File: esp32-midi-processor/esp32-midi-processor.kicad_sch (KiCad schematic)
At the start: 50 parts, among them J1 Midi IN 1, J10 USB Shield right, J11 Spare, J12 Display, J2 Midi IN 2, J3 Midi OUT 1, J4 Midi OUT 2, J5 ESP32 right, J6 ESP32 left, J7 Input Voltage, J8 USB Shield outer left, J9 USB Shield inner left, SW1 SW_Push, SW2 SW_Push, SW3 SW_Push, SW4 SW_Push, SW5 RotaryEncoder_Switch, U1 6N138, U2 6N138

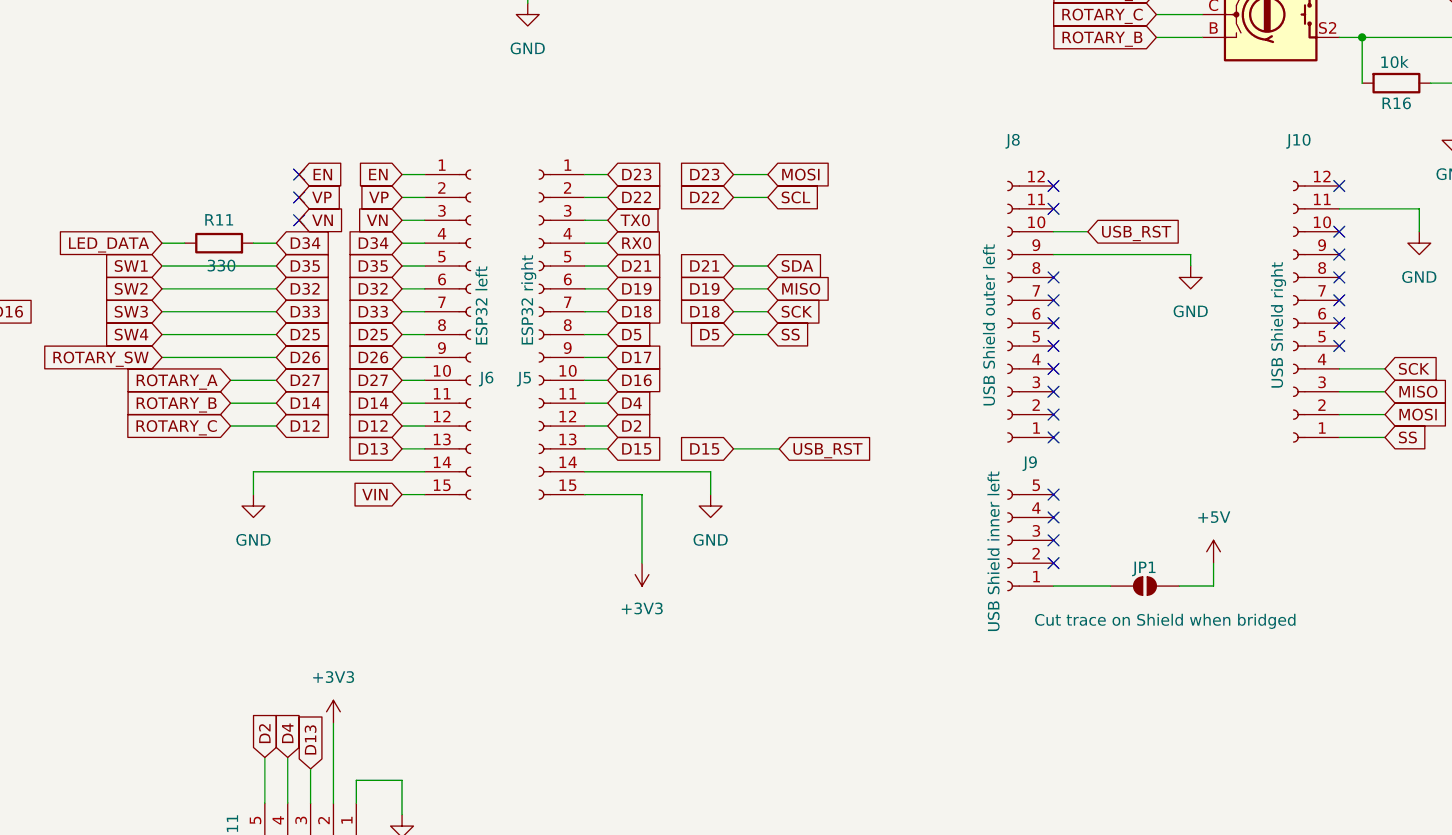
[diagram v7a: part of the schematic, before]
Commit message: fix orientation of pinheaders
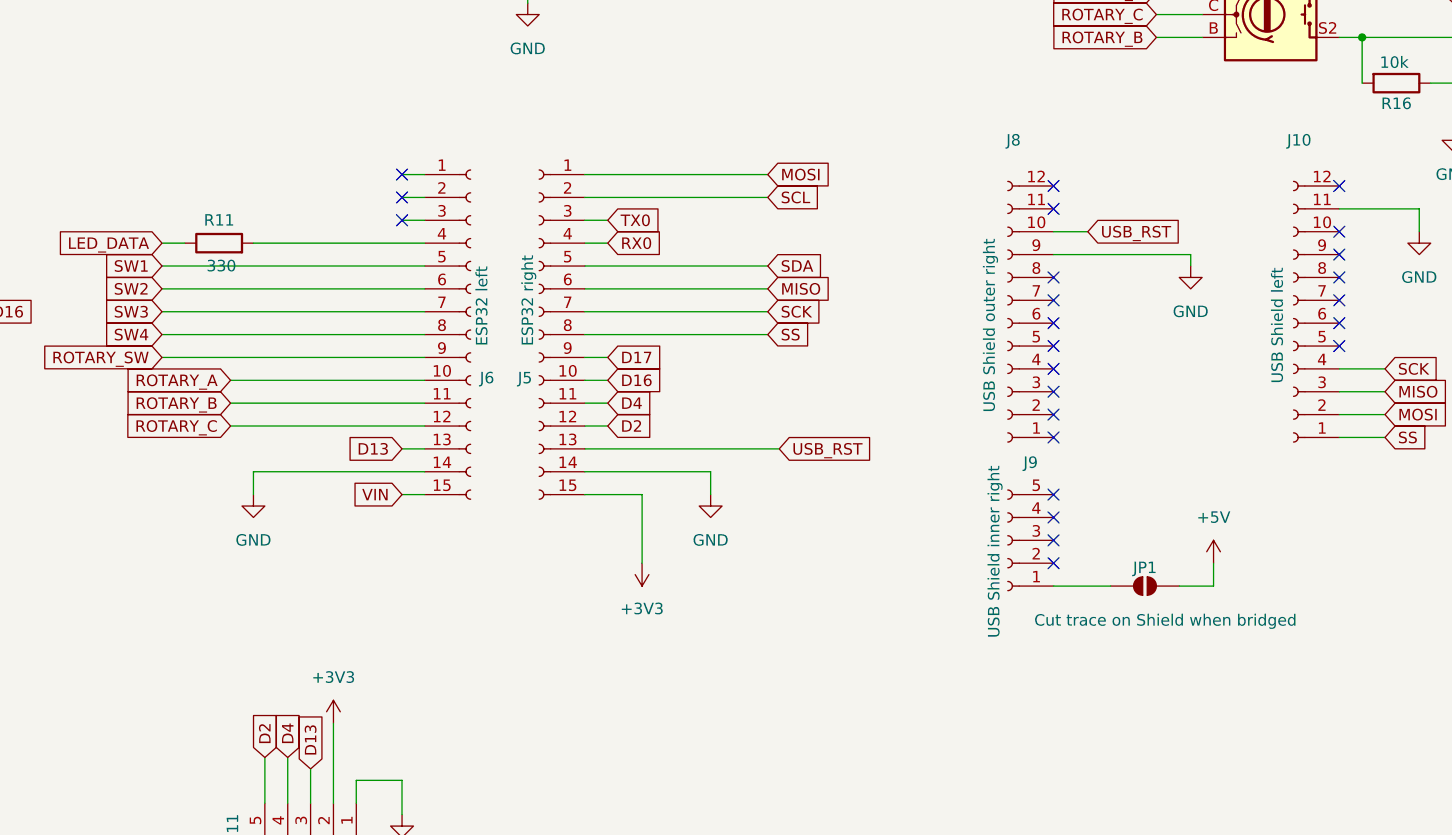
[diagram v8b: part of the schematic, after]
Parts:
- J10: value USB Shield right -> USB Shield left
- J8: value USB Shield outer left -> USB Shield outer right
- J9: value USB Shield inner left -> USB Shield inner right
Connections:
- net D12 renamed ROTARY_C
- net D14 renamed ROTARY_B
- net D15 renamed USB_RST
- net D18 renamed SCK
- net D19 renamed MISO
- net D21 renamed SDA
- net D22 renamed SCL
- net D23 renamed MOSI
- net D25 renamed SW4
- net D26 renamed ROTARY_SW
- net D27 renamed ROTARY_A
- net D32 renamed SW2
- net D33 renamed SW3
- net D34: no longer names the net of J6.4 (Pin_4), R11.2
- net D35 renamed SW1
- net D5 renamed SS
- net EN: no longer names the net of J6.1 (Pin_1)
- net VN: no longer names the net of J6.3 (Pin_3)
- net VP: no longer names the net of J6.2 (Pin_2)
